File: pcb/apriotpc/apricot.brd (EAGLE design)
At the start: 31 x 90 mm, 16 parts, among them J2 ATX24RH

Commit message: added apricot pc
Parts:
- moved C2 2.51 mm to (10.4, 85.1)
- moved C5 2.04 mm to (27.2, 62.9)
- moved C6 2.02 mm to (26.2, 67.4)
- moved C1 2.00 mm to (27.0, 18.8)
- moved C7 2.00 mm to (27.2, 27.3)
- moved C8 2.00 mm to (26.1, 22.9)
- moved J2 2.00 mm to (9.00, 45.0)
- moved JP1 2.00 mm to (27.0, 7.37)
- moved JP3 2.00 mm to (25.1, 86.1)
- moved U$1 2.00 mm to (15.5, 85.0)
- moved U$2 2.00 mm to (10.0, 75.0)
- moved U$3 2.00 mm to (15.5, 5.00)
- moved U$4 2.00 mm to (26.8, 45.0)
- moved U$8 2.00 mm to (10.0, 15.0)
- moved C3 2.00 mm to (3.81, 85.6)
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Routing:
- net +12V: track 112.5 -> 113.4 mm

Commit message: adjusted holes
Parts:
- moved JP3 2.96 mm to (27.2, 84.0), turned to 270 degrees
- moved U$1 2.00 mm to (17.5, 85.0)
- moved U$3 2.00 mm to (17.5, 5.00)
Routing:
- net N$1: track 42.8 -> 43.6 mm
- net +12V: track 113.4 -> 114.0 mm
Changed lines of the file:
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@@
 <setting verticaltext="up"/>
 </settings>
-<grid distance="1" unitdist="mm" unit="mm" style="lines" multiple="1" display="no" altdistance="1" altunitdist="mil" altunit="mil"/>
+<grid distance="5" unitdist="mil" unit="mm" style="lines" multiple="1" display="no" altdistance="1" altunitdist="mil" altunit="mil"/>
 <layers>
 <layer number="1" name="Top" color="4" fill="1" visible="yes" active="yes"/>
@@
 <element name="U$2" library="atx_power_control" package="FUSE_HOLDER_3IN1" value="CAR_FUSE_HOLDER3IN1" x="10" y="75" smashed="yes"/>
 <element name="J2" library="macse" package="ATX24_RIGHT_ANGLE" value="ATX24RH" x="9" y="45" smashed="yes" rot="R270"/>
-<element name="JP3" library="appleii" package="1X04" value="" x="25.051" y="86.106" smashed="yes"/>
-<element name="U$1" library="a" package="M3_MOUNTING_HOLE_PACK" value="M3_MOUNTING_HOLE" x="15.5" y="85" smashed="yes"/>
-<element name="U$3" library="a" package="M3_MOUNTING_HOLE_PACK" value="M3_MOUNTING_HOLE" x="15.5" y="5" smashed="yes"/>
+<element name="JP3" library="appleii" package="1X04" value="" x="27.178" y="84.042" smashed="yes" rot="R270"/>
+<element name="U$1" library="a" package="M3_MOUNTING_HOLE_PACK" value="M3_MOUNTING_HOLE" x="17.5" y="85" smashed="yes"/>
+<element name="U$3" library="a" package="M3_MOUNTING_HOLE_PACK" value="M3_MOUNTING_HOLE" x="17.5" y="5" smashed="yes"/>
 <element name="C2" library="capacitor-wima" library_urn="urn:adsk.eagle:library:116" package="C5B2.5" package3d_urn="urn:adsk.eagle:package:5426/1" value="" x="10.414" y="85.09" smashed="yes" rot="R90">
 <attribute name="NAME" x="13.748" y="89.249" size="1.27" layer="25" ratio="10" rot="R180"/>
@@
 <wire x1="21.114" y1="76.454" x2="29.75" y2="76.454" width="1.778" layer="16"/>
 <wire x1="29.75" y1="76.454" x2="29.75" y2="72.517" width="1.778" layer="16"/>
-<wire x1="23.781" y1="80.137" x2="23.781" y2="86.106" width="1.778" layer="16"/>
-<wire x1="21.114" y1="80.137" x2="23.781" y2="80.137" width="1.778" layer="16"/>
 <wire x1="22.257" y1="69.977" x2="22.257" y2="51.689" width="1.778" layer="16"/>
 <wire x1="24.986" y1="48.96" x2="26.798" y2="48.96" width="1.778" layer="16"/>
 <wire x1="22.257" y1="51.689" x2="24.986" y2="48.96" width="1.778" layer="16"/>
+<wire x1="27.178" y1="85.312" x2="24.606" y2="85.312" width="1.778" layer="16"/>
+<wire x1="24.606" y1="85.312" x2="23.241" y2="83.947" width="1.778" layer="16"/>
+<wire x1="23.241" y1="83.947" x2="23.241" y2="82.264" width="1.778" layer="16"/>
+<wire x1="23.241" y1="82.264" x2="21.114" y2="80.137" width="1.778" layer="16"/>
 </signal>
 <signal name="N$1">
@@
 <wire x1="19.26" y1="34.5" x2="16.542" y2="31.782" width="0.3048" layer="16"/>
 <wire x1="16.542" y1="20.574" x2="14.383" y2="18.415" width="0.3048" layer="16"/>
-<wire x1="14.383" y1="18.415" x2="14.383" y2="11.938" width="0.3048" layer="16"/>
-<wire x1="18.701" y1="7.62" x2="26.575" y2="7.62" width="0.3048" layer="16"/>
-<wire x1="26.575" y1="7.62" x2="28.258" y2="9.303" width="0.3048" layer="16"/>
-<wire x1="28.258" y1="9.303" x2="28.258" y2="11.176" width="0.3048" layer="16"/>
+<wire x1="14.383" y1="18.415" x2="14.383" y2="11.684" width="0.3048" layer="16"/>
 <wire x1="16.542" y1="31.782" x2="16.542" y2="20.574" width="0.3048" layer="16"/>
-<wire x1="14.383" y1="11.938" x2="18.701" y2="7.62" width="0.3048" layer="16"/>
+<wire x1="14.383" y1="11.684" x2="15.526" y2="10.541" width="0.3048" layer="16"/>
+<wire x1="28.258" y1="13.398" x2="28.258" y2="11.176" width="0.3048" layer="16"/>
+<wire x1="15.526" y1="10.541" x2="19.558" y2="10.541" width="0.3048" layer="16"/>
+<wire x1="19.558" y1="10.541" x2="23.622" y2="14.605" width="0.3048" layer="16"/>
+<wire x1="23.622" y1="14.605" x2="27.051" y2="14.605" width="0.3048" layer="16"/>
+<wire x1="27.051" y1="14.605" x2="28.258" y2="13.398" width="0.3048" layer="16"/>
 </signal>
 <signal name="N$2">

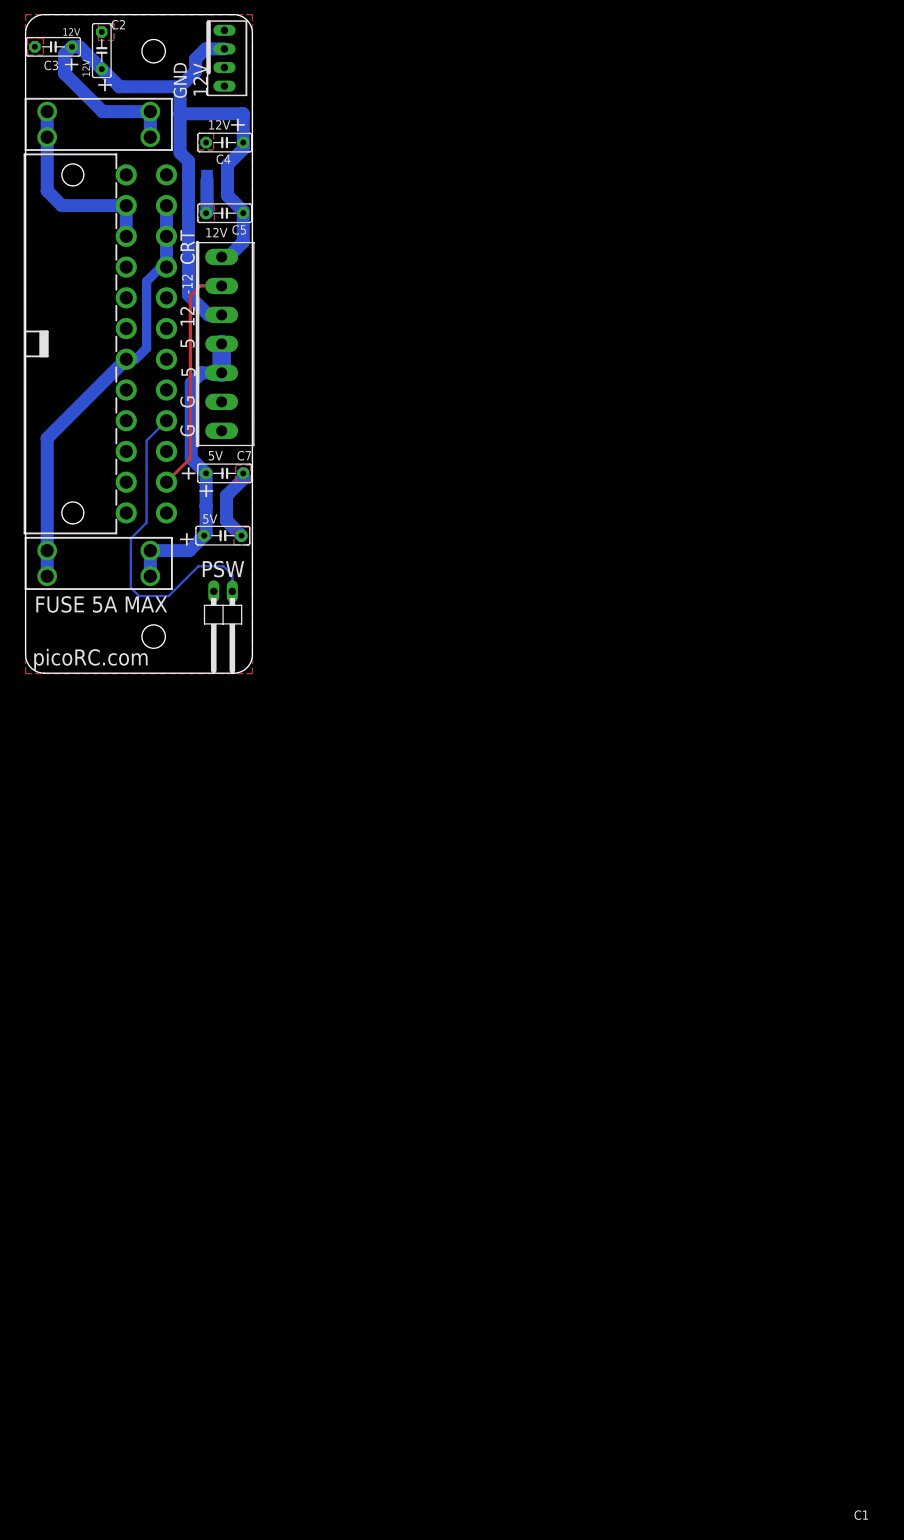
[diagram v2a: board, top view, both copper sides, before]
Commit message: added grounding blade and exposed screw pad, added psw blade
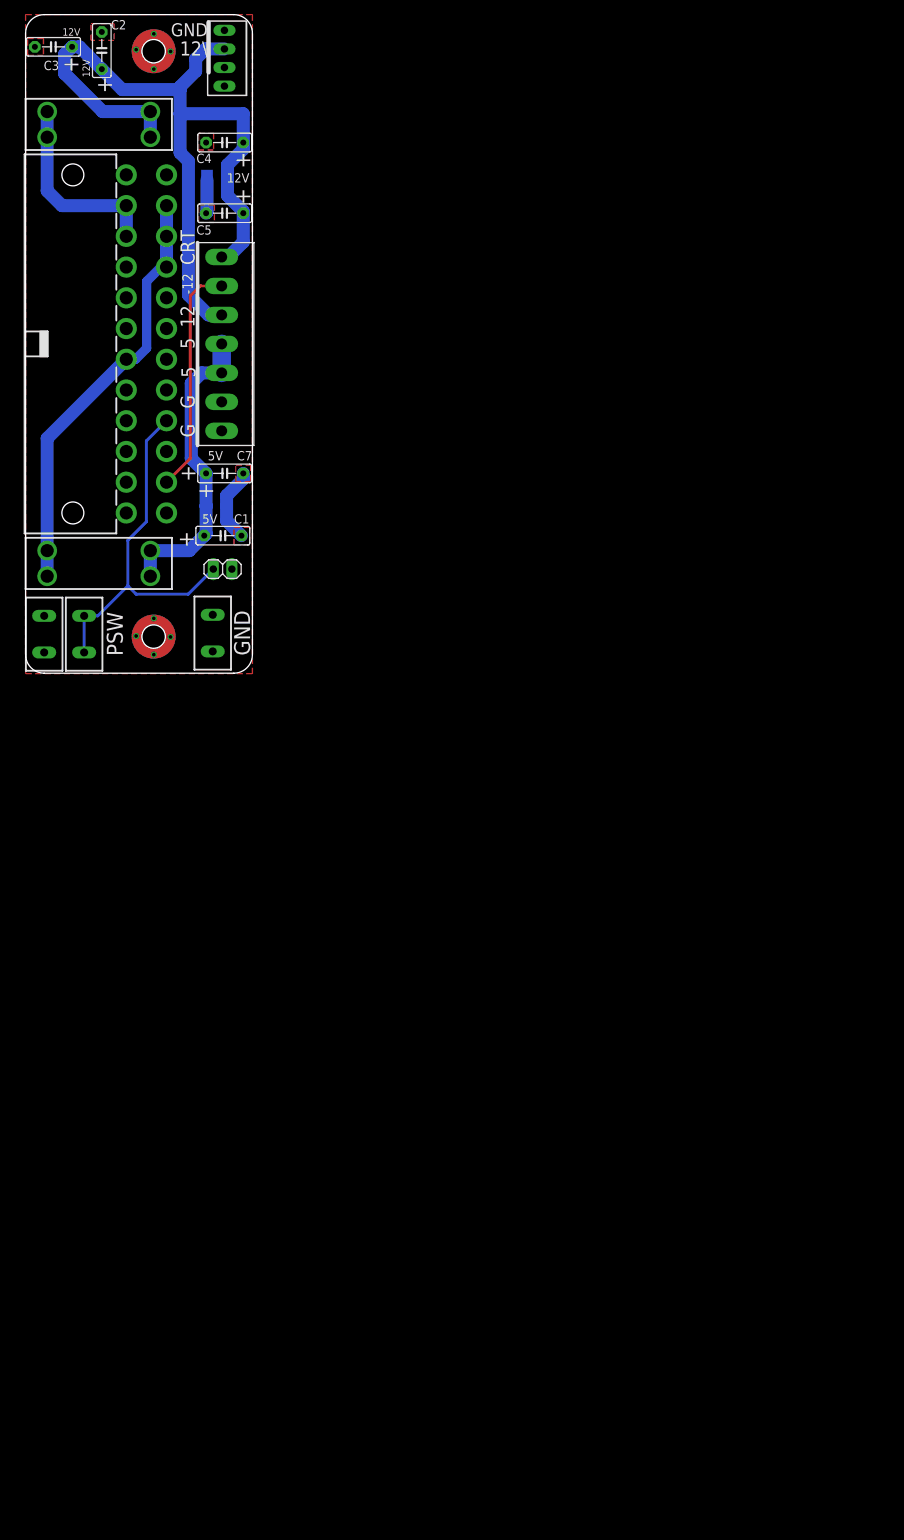
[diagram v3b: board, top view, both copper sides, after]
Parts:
- added U$5, U$6: M3_MOUNTING_HOLE, apricot:M3_MOUNTING_HOLE_PACK
- added U$7: 6MM_BLADE, apricot:6.2MMBLADE
- JP1: device pinhead:1X02/90 -> pinhead:1X02
- U$1, U$3: value M3_MOUNTING_HOLE -> 6MM_BLADE; device a:M3_MOUNTING_HOLE_PACK -> apricot:6.2MMBLADE
- moved U$1 80.2 mm to (8.00, 5.33), turned to 270 degrees
- moved U$3 15.0 mm to (2.54, 5.33), turned to 270 degrees
- moved JP1 6.86 mm to (26.9, 14.2)
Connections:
- net GND: now also JP1.1, U$3.P$1, U$3.P$2, U$5.P$1, U$5.P$2, U$6.P$1, U$6.P$2, U$7.P$1, U$7.P$2; no longer JP1.2
- net N$1: now also JP1.2, U$1.P$1, U$1.P$2; no longer JP1.1
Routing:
- net N$1: track 43.6 -> 51.0 mm
- net GND: vias 0 -> 8
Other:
- board text added: "12\"
- board text added: "dekuNukem 2023 picoRC.com"
- board text removed: "picoRC.com"

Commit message: adjust apricot pc resistors
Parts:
- added C10, C12: 100nF, clock:0805@1
- added C11, C9: (no value), adafruit:E5-10,5
- C3, C7: value (none) -> 100nF; device capacitor-wima:C5B2.5 -> clock:0805@1
- C4: device capacitor-wima:C5B2.5 -> adafruit:E5-10,5
- moved C3 27.5 mm to (26.8, 70.5), flipped to the bottom, turned to 0 degrees
- moved C4 26.2 mm to (4.06, 84.8)
- moved C6 8.77 mm to (26.6, 76.2), turned to 180 degrees
- moved C5 2.92 mm to (27.1, 65.8), turned to 0 degrees
- moved C7 2.35 mm to (26.7, 29.6), flipped to the bottom
- moved C8 0.72 mm to (26.6, 22.4)
- moved C2 0.38 mm to (10.8, 85.1)
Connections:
- net +12V: now also C10.2, C3.2, C4.+, C9.+; no longer C3.1, C4.1
- net +5V: now also C11.+, C12.2, C7.2; no longer C7.1
- net GND: now also C10.1, C11.-, C12.1, C3.1, C4.-, C7.1, C9.-; no longer C3.2, C4.2, C7.2
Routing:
- net GND: track 14.9 -> 37.9 mm
- net +12V: track 114.2 -> 107.1 mm
- net +5V: track 42.2 -> 45.1 mm

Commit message: fixed connector oritation
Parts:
- moved JP1 1.80 mm to (25.7, 13.0)
- moved C1 1.27 mm to (27.0, 17.5)
- moved C11 1.27 mm to (26.5, 24.4)
- moved C12 1.27 mm to (26.7, 26.5)
- moved C7 1.27 mm to (26.7, 28.3)
- moved C8 1.27 mm to (26.6, 21.1)
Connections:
- net +12V: now also U$4.P$1, U$4.P$3; no longer U$4.P$5, U$4.P$7
- net +5V: now also U$4.P$5; no longer U$4.P$3
- net GND: now also U$4.P$6, U$4.P$7; no longer U$4.P$1, U$4.P$2
- net N$2: now also U$4.P$2; no longer U$4.P$6
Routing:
- net +12V: track 107.1 -> 143.6 mm
- net N$2: track 31.7 -> 15.0 mm
- net +5V: track 45.1 -> 52.1 mm
- net N$1: track 51.0 -> 49.2 mm
